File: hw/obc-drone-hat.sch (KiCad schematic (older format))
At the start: 0 parts

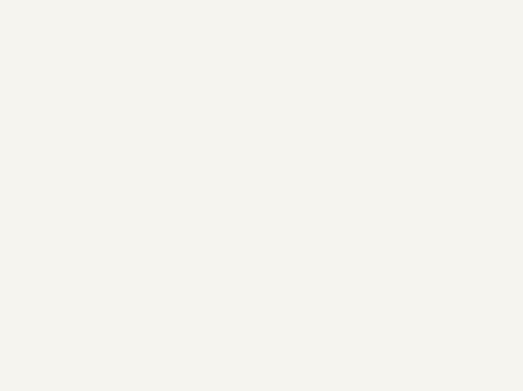
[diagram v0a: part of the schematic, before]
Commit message: switch to KiCAD 5 (nightly)
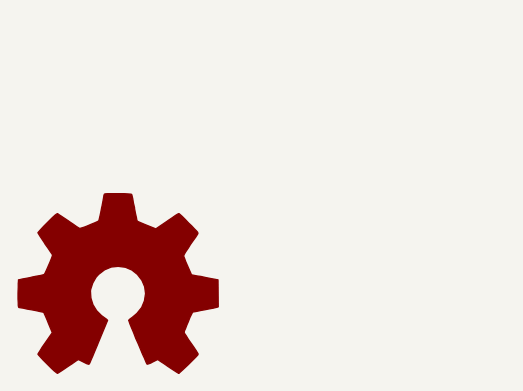
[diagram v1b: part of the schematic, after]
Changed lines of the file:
@@
-EESchema Schematic File Version 2
-LIBS:power
-LIBS:device
-LIBS:transistors
-LIBS:conn
-LIBS:linear
-LIBS:regul
-LIBS:74xx
-LIBS:cmos4000
-LIBS:adc-dac
-LIBS:memory
-LIBS:xilinx
-LIBS:microcontrollers
-LIBS:dsp
-LIBS:microchip
-LIBS:analog_switches
-LIBS:motorola
-LIBS:texas
-LIBS:intel
-LIBS:audio
-LIBS:interface
-LIBS:digital-audio
-LIBS:philips
-LIBS:display
-LIBS:cypress
-LIBS:siliconi
-LIBS:opto
-LIBS:atmel
-LIBS:contrib
-LIBS:valves
-LIBS:rpi_con
-LIBS:ic
-LIBS:dronecode_con
+EESchema Schematic File Version 4
 LIBS:obc-drone-hat-cache
-EELAYER 25 0
+EELAYER 26 0
 EELAYER END
 $Descr A3 16535 11693
@@
 F1 "dc-dc.sch" 60
 $EndSheet
+$Comp
+L Graphic:Logo_Open_Hardware_Large #LOGO?
+U 1 1 5AB63E41
+P 1450 10950
+F 0 "#LOGO?" H 1450 11450 50  0001 C CNN
+F 1 "Logo_Open_Hardware_Large" H 1450 10550 50  0001 C CNN
+F 2 "" H 1450 10950 50  0001 C CNN
+F 3 "~" H 1450 10950 50  0001 C CNN
+	1    1450 10950
+	1    0    0    -1
+$EndComp
 $EndSCHEMATC

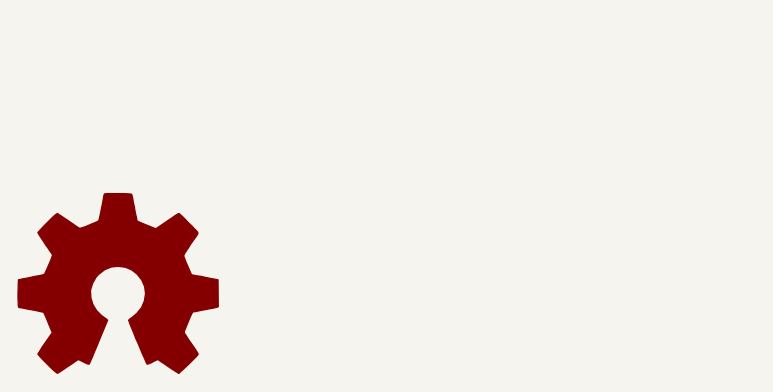
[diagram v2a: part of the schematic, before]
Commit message: hw: add mounting holes
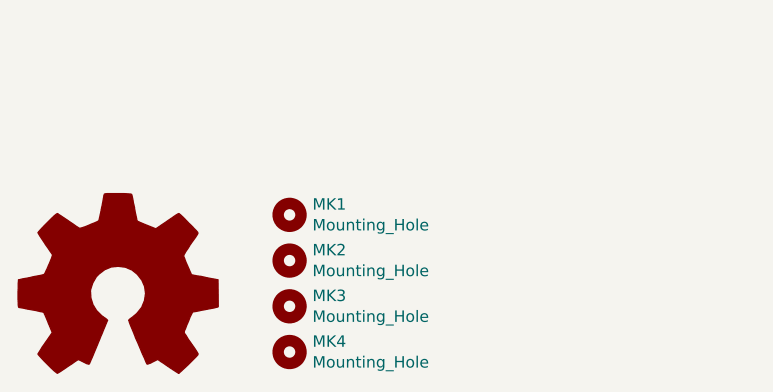
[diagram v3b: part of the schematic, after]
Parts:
- added MK1, MK2, MK3, MK4: Mounting_Hole, hat:M2.5_Mounting_Hole, symbol Mechanical:Mounting_Hole
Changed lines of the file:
@@
+	1    0    0    -1
+$EndComp
+$Comp
+L Mechanical:Mounting_Hole MK1
+U 1 1 5ACC54BA
+P 2200 10600
+F 0 "MK1" H 2300 10646 50  0000 L CNN
+F 1 "Mounting_Hole" H 2300 10555 50  0000 L CNN
+F 2 "hat:M2.5_Mounting_Hole" H 2200 10600 50  0001 C CNN
+F 3 "" H 2200 10600 50  0001 C CNN
+	1    2200 10600
+	1    0    0    -1
+$EndComp
+$Comp
+L Mechanical:Mounting_Hole MK2
+U 1 1 5ACC5819
+P 2200 10800
+F 0 "MK2" H 2300 10846 50  0000 L CNN
+F 1 "Mounting_Hole" H 2300 10755 50  0000 L CNN
+F 2 "hat:M2.5_Mounting_Hole" H 2200 10800 50  0001 C CNN
+F 3 "" H 2200 10800 50  0001 C CNN
+	1    2200 10800
+	1    0    0    -1
+$EndComp
+$Comp
+L Mechanical:Mounting_Hole MK3
+U 1 1 5ACC5831
+P 2200 11000
+F 0 "MK3" H 2300 11046 50  0000 L CNN
+F 1 "Mounting_Hole" H 2300 10955 50  0000 L CNN
+F 2 "hat:M2.5_Mounting_Hole" H 2200 11000 50  0001 C CNN
+F 3 "" H 2200 11000 50  0001 C CNN
+	1    2200 11000
+	1    0    0    -1
+$EndComp
+$Comp
+L Mechanical:Mounting_Hole MK4
+U 1 1 5ACC584F
+P 2200 11200
+F 0 "MK4" H 2300 11246 50  0000 L CNN
+F 1 "Mounting_Hole" H 2300 11155 50  0000 L CNN
+F 2 "hat:M2.5_Mounting_Hole" H 2200 11200 50  0001 C CNN
+F 3 "" H 2200 11200 50  0001 C CNN
+	1    2200 11200
 	1    0    0    -1
 $EndComp
